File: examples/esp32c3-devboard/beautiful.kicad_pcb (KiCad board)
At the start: 2 copper layers, 30 x 60 mm, 31 parts, among them J1 GPIO-A, J2 GPIO-B, J3 USB-C, SW1 RESET, SW2 BOOT, U1 ESP32-C3-WROOM-02, U2 AP2112K-3.3, U3 USBLC6-2SC6

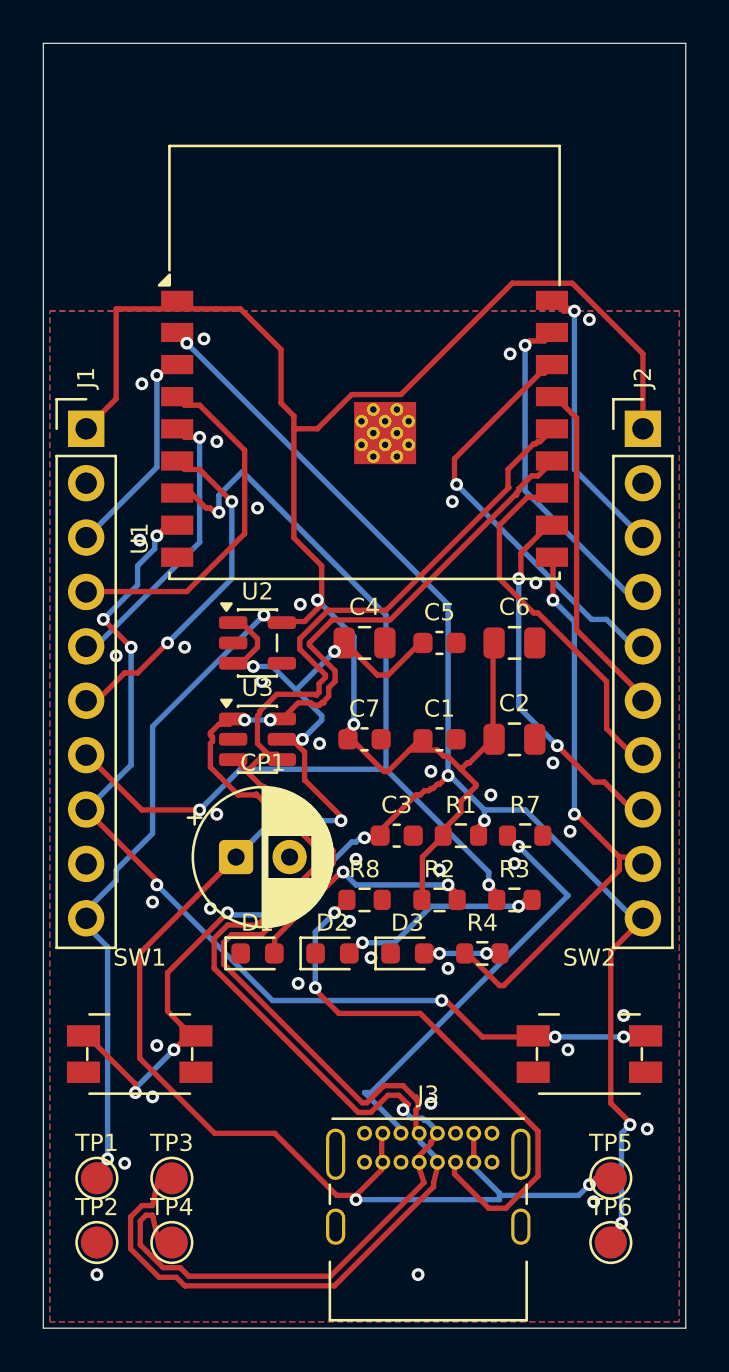
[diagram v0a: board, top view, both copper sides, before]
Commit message: Update example board: DRC clean, antenna keepout enforced, USB routed as a pair
The example now ships the finished board rather than a mid-flight one: 0 DRC
errors, 0 unconnected pads, 5 of 6 checks passing. The remaining failure (USB
diff-pair via asymmetry) is documented as accepted, with the reason the router
cannot fix it - it is a placement problem, not a routing one.

Co-Authored-By: Claude Opus 5 <noreply@anthropic.com>
Claude-Session: https://claude.ai/code/session_01ALwmbGyCjoQJCkYJDeXGjc
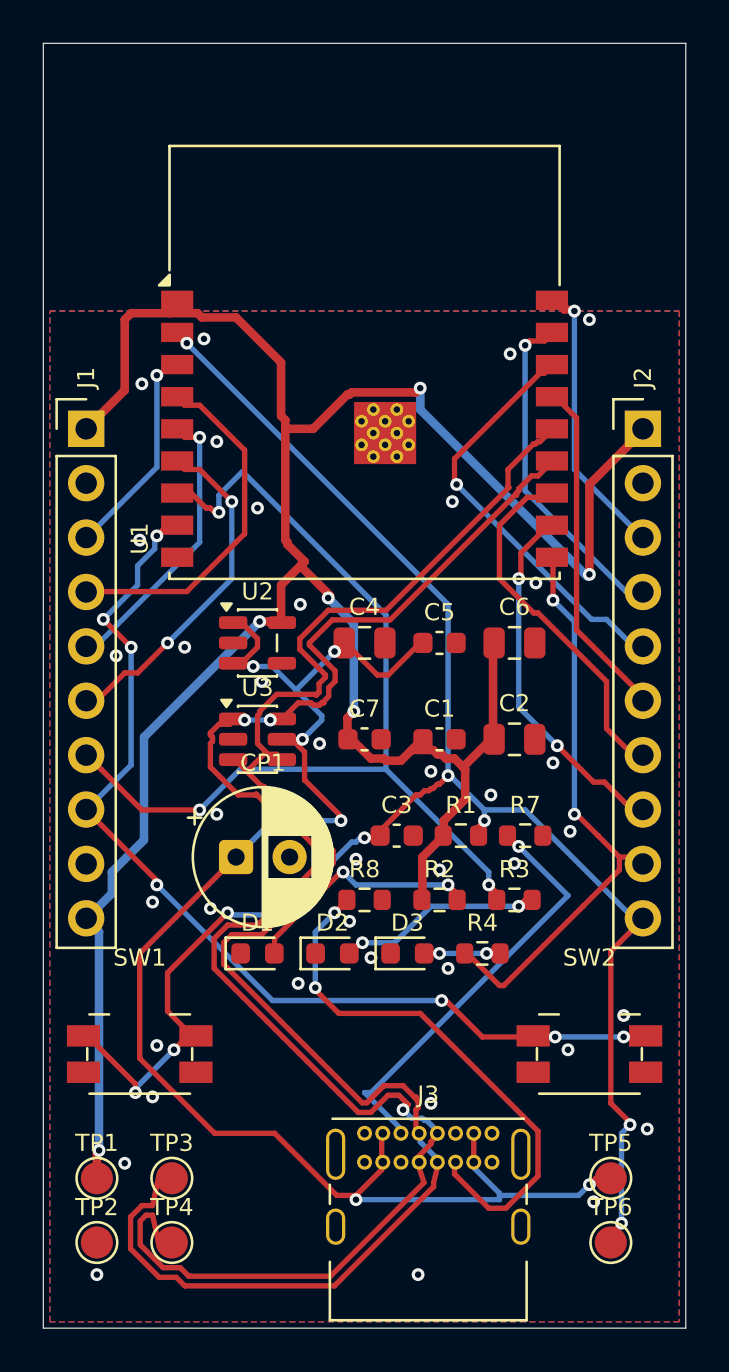
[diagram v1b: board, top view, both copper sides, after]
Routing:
- net +3V3: track 113.7 -> 115.4 mm, vias 4 -> 6

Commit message: Fix decoupling model, derive placement freedoms, add targeted relocation
Generalises an edge case found on the example board: the ESP32's 3V3 pin sat
22 mm from its nearest 100 nF capacitor while the optimiser reported a near-zero
decoupling violation. Four separate causes, each fixed generally rather than for
this board.

Decoupling is now scored per power PIN, not per capacitor, measured pad-to-pad
on the rail. Per-capacitor scoring lets every cap cluster around one convenient
pin and report success while another pin is starved - which is exactly what
happened. Pad-to-pad is the real trace length, and with the ground return it is
the loop area that decides whether the capacitor does anything.

Placement freedoms are derived from geometry instead of listed by hand:
- an anchor sitting on a board edge may slide ALONG that edge, because a
  connector is fixed to stay reachable - that pins one axis, not two
- a part owning a footprint keepout stays pinned, since the keepout is anchored
  in board coordinates and moving the part would decouple an RF module from its
  antenna exclusion zone
- a keepout owner's courtyard is clipped to its physical body for overlap
  testing; some footprints draw the courtyard around the keepout too, making an
  RF module appear to collide with everything near it

Added a targeted relocation operator. A random walk never makes a 12 mm jump
because every intermediate position is worse, so the search plateaued with a pin
unserved while 66 legal positions sat empty within 8 mm of it. 18% of proposals
now pick the worst-served power pin and move a suitable capacitor directly to a
legal spot beside it.

Example board re-optimised and re-routed: copper 772.4 -> 661.0 mm, vias 92 ->
42, ESP32 3V3 pin to nearest 100 nF 22.00 -> 4.09 mm, 0 DRC errors, all 23 nets
routed. USB pair skew went 1.52 -> 2.89 mm - the one term that got worse.

Adds a repo social preview rendered from the board's own F.Cu layer.

Co-Authored-By: Claude Opus 5 <noreply@ant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
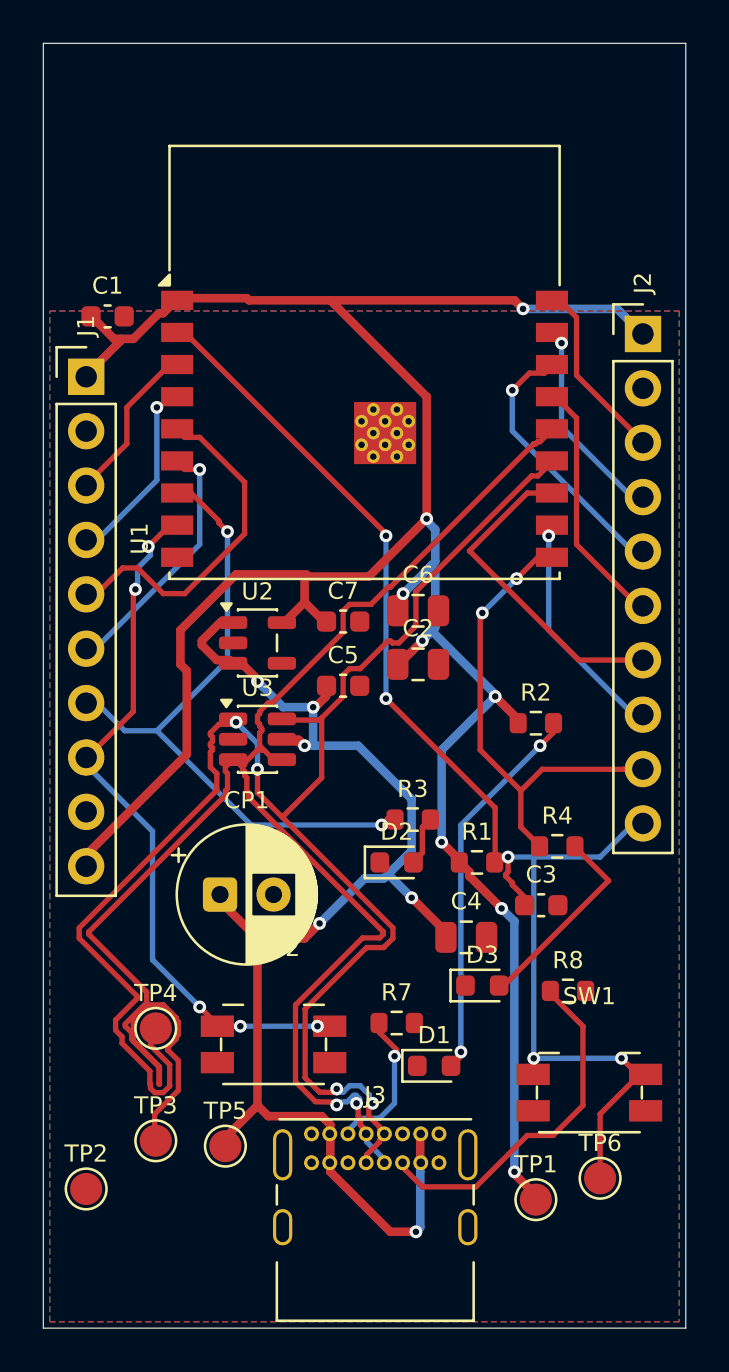
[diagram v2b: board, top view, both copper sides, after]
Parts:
- moved C1 25.1 mm to (103.0, 62.8)
- moved SW1 21.1 mm to (125.5, 99.0)
- moved TP1 20.5 mm to (123.0, 104.0)
- moved TP5 18.1 mm to (108.5, 101.5)
- moved SW2 14.8 mm to (110.8, 96.8)
- moved C4 14.5 mm to (119.8, 91.8)
- moved R7 10.6 mm to (116.5, 95.8)
- moved R8 10.4 mm to (124.5, 94.2)
- moved TP4 10.0 mm to (105.2, 96.0)
- moved D1 9.78 mm to (118.2, 97.8)
- moved R2 9.40 mm to (123.0, 81.8)
- moved C3 7.49 mm to (123.2, 90.2)
- moved R4 6.10 mm to (124.0, 87.5)
- moved R3 6.05 mm to (117.2, 86.2)
- moved C2 5.70 mm to (117.5, 79.0)
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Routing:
- net EN: track 83.4 -> 61.7 mm, vias 9 -> 5
- net IO8: track 45.6 -> 30.9 mm, vias 3 -> 2
- net IO9: track 46.9 -> 32.7 mm, vias 7 -> 5
- net CC1: track 19.9 -> 6.73 mm
- net CC2: track 25.8 -> 16.6 mm, vias 2 -> 0
- net IO5: track 16.7 -> 7.91 mm, vias 0 -> 1
- net VBUS: track 72.3 -> 64.3 mm
- net LED_IO8: track 9.46 -> 2.44 mm, vias 2 -> 0
- net PWR_LED: track 11.1 -> 18.1 mm
- net IO20_RXD: track 17.0 -> 10.5 mm, vias 2 -> 1
- net IO2: track 19.0 -> 12.8 mm
- net IO1: track 15.8 -> 9.68 mm
- net LED_IO10: track 3.53 -> 9.42 mm, vias 2 -> 0
- net IO0: track 14.3 -> 8.57 mm, vias 1 -> 0
- net USB_DP: track 79.5 -> 85.2 mm, vias 0 -> 2
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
